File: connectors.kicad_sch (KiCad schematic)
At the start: 10 parts, among them J3 Conn_01x23, J4 Conn_01x14, U3 ULN2003A

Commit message: started adding AD2S
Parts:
- C16: renamed from C?; value (none) -> 10uF; footprint (none) -> Capacitor_SMD:C_0603_1608Metric; symbol prius_gen2-rescue:C-Device-prius_gen2-rescue -> Device:C
- C17: renamed from C19; symbol prius_gen2-rescue:C-Device-prius_gen2-rescue -> Device:C
- R14: renamed from R?; value (none) -> 510; footprint (none) -> Resistor_SMD:R_0603_1608Metric; symbol prius_gen2-rescue:R-Device-prius_gen2-rescue -> Device:R
- R15: renamed from R?; value (none) -> 220; footprint (none) -> Resistor_SMD:R_0603_1608Metric; symbol prius_gen2-rescue:R-Device-prius_gen2-rescue -> Device:R
- R16: renamed from R24; symbol prius_gen2-rescue:R-Device-prius_gen2-rescue -> Device:R
- R17: renamed from R25; symbol prius_gen2-rescue:R-Device-prius_gen2-rescue -> Device:R
- R18: renamed from R26; symbol prius_gen2-rescue:R-Device-prius_gen2-rescue -> Device:R
- renumbered U3 to U2
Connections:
- net CPWM: no longer names the net of J4.8 (Pin_8)
- net CPWM: no longer U2.13 (O4)
- net OUT_DCSW: no longer names the net of J3.15 (Pin_15)
- net OUT_PRE: no longer names the net of J3.16 (Pin_16)
- net SIG_BRAKE: no longer names the net of J3.10 (Pin_10)
- net SIG_FWD: no longer names the net of J3.11 (Pin_11)
- net SIG_REV: no longer names the net of J3.12 (Pin_12)
- net SIG_START: no longer names the net of J3.9 (Pin_9)
- net THROTTLE1: no longer names the net of J3.7 (Pin_7)
- net THROTTLE2: no longer names the net of J3.8 (Pin_8)
- net TIM1_CH2N: no longer names the net of U2.4 (I4)
- no-connect marks 3 -> 14

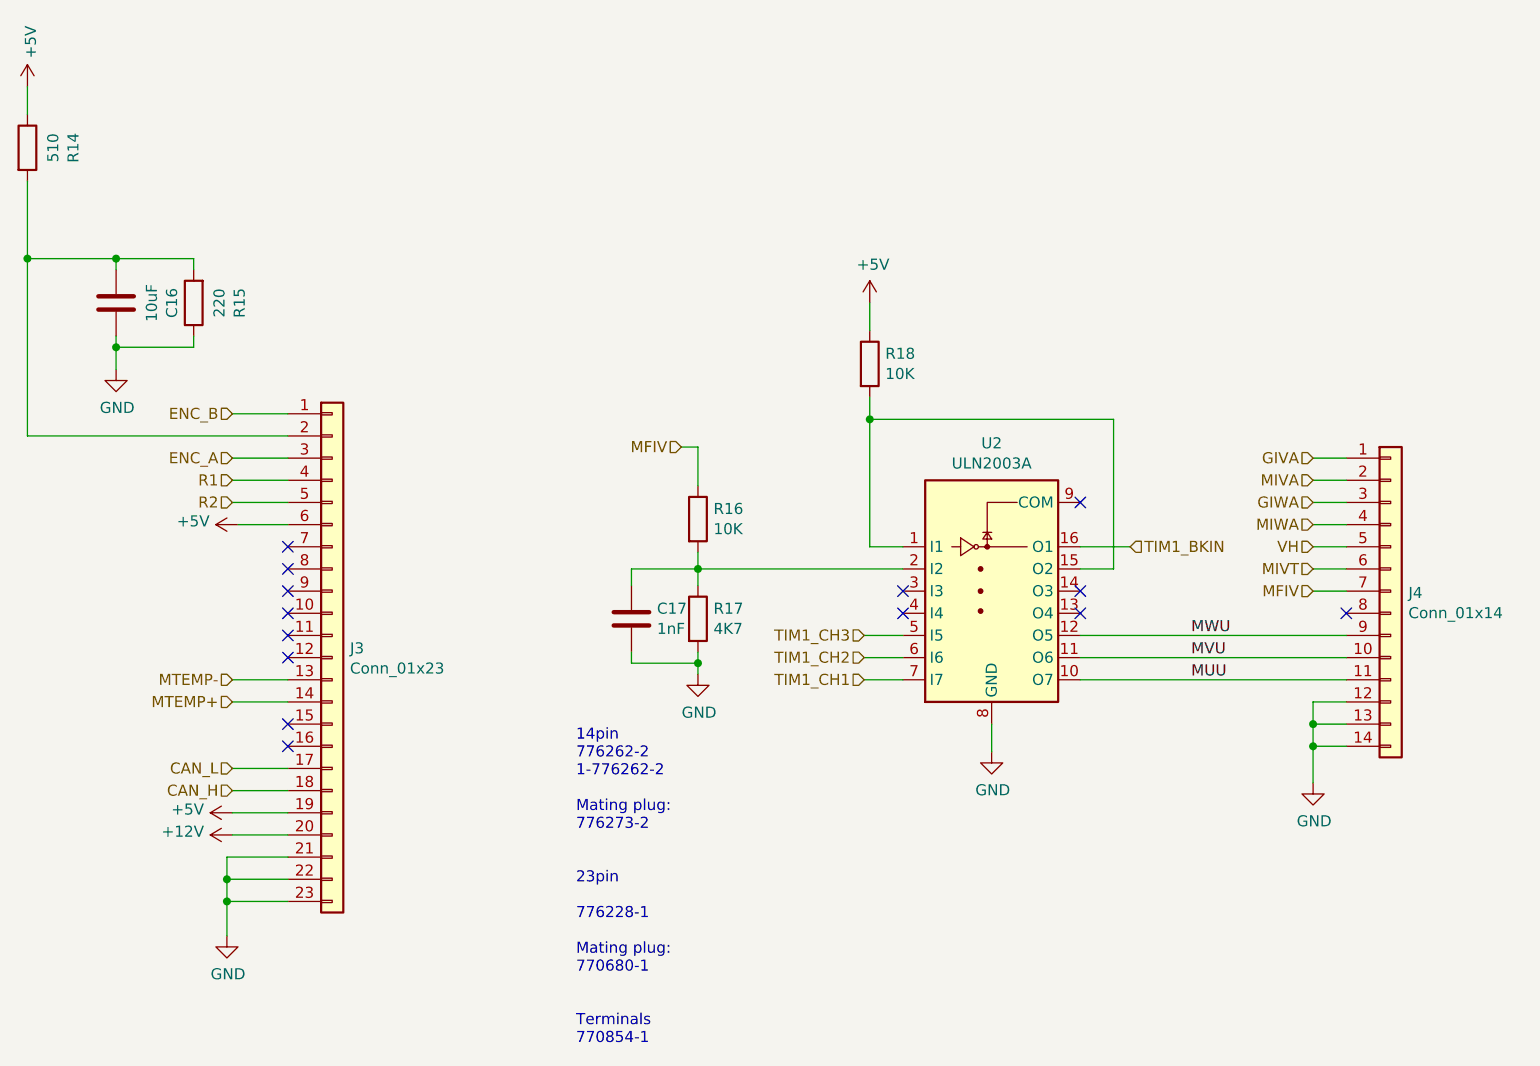
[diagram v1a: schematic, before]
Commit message: routed ad2s
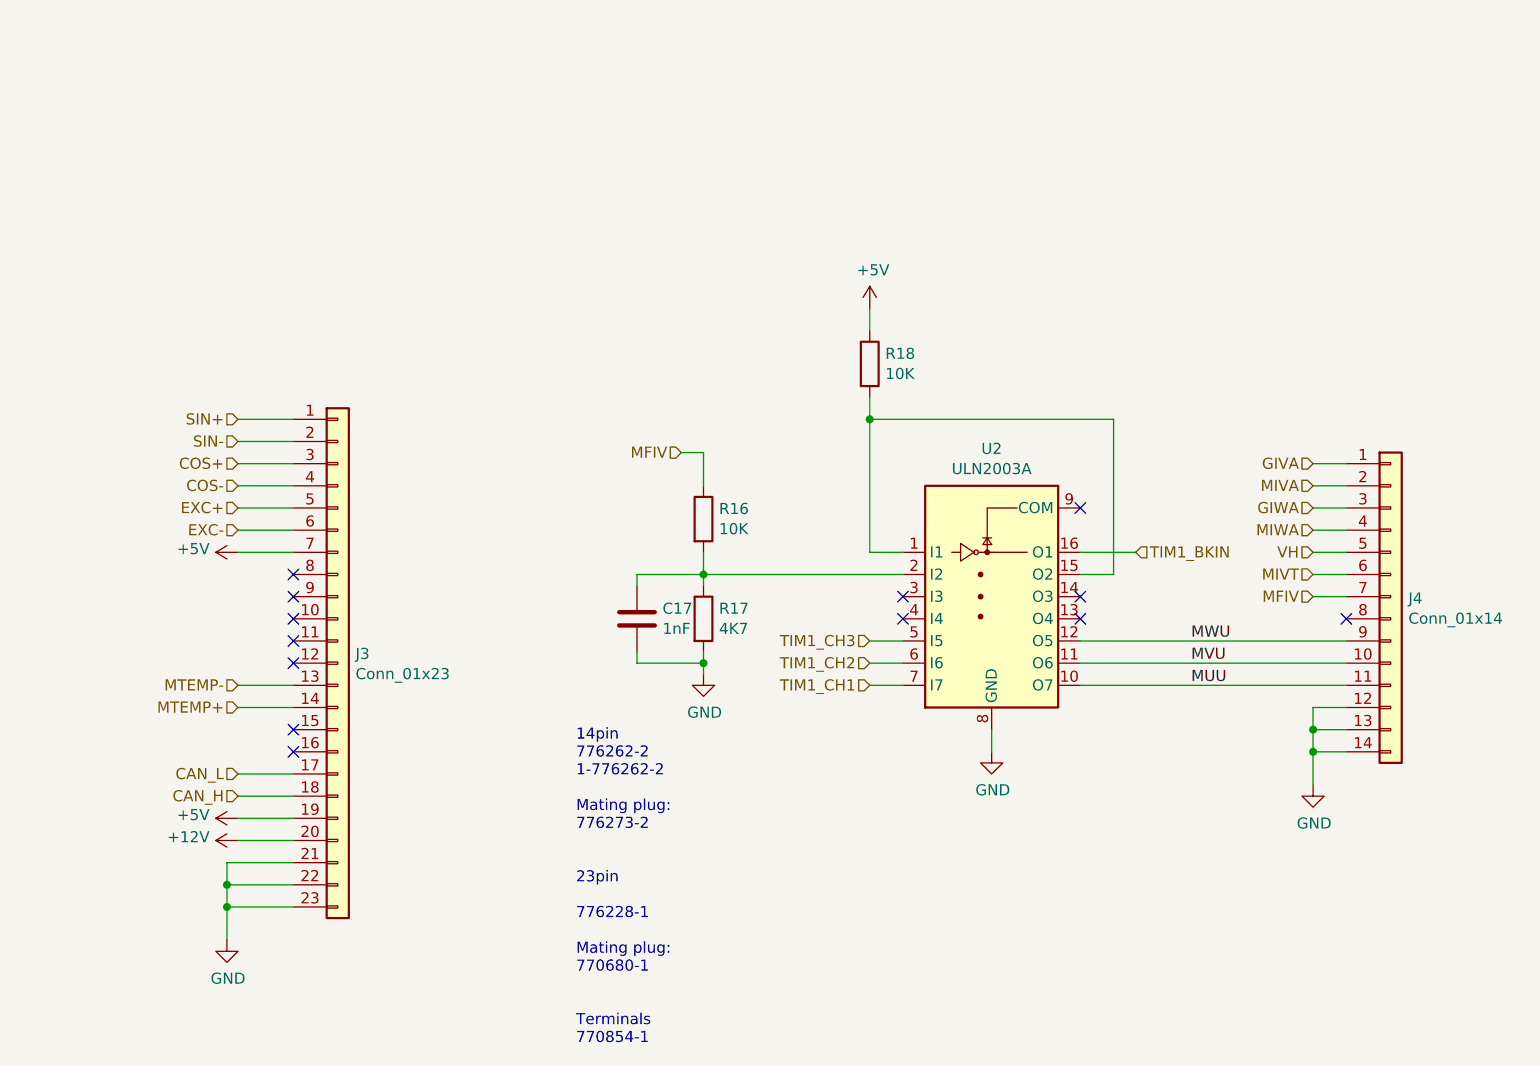
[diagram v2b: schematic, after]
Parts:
- removed C16: 10uF, Capacitor_SMD:C_0603_1608Metric, symbol Device:C
- removed R14: 510, Resistor_SMD:R_0603_1608Metric, symbol Device:R
- removed R15: 220, Resistor_SMD:R_0603_1608Metric, symbol Device:R
- R16, R18: LCSC (none) -> C25804
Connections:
- net +5V: now also J3.7 (Pin_7); no longer J3.6 (Pin_6)
- net SIN-: now reaches J3.2 (Pin_2)
- net ENC_A renamed COS+
- net ENC_B renamed SIN+
- net R1 renamed COS-
- net R2 renamed EXC+
- new net EXC-: J3.6 (Pin_6)
- no-connect marks 14 -> 13
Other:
- moved on the sheet: C17, J3, J4, R16, R17, U2
